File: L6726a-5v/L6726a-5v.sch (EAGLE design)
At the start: 28 parts, among them IC1 L6727A, U1 5V

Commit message: finalized layout, I think I'm happy
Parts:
- removed U1: 5V, SparkFun-PowerIC:V_REG_317SMD
- added IC2: MCP1804, microchip-vreg:MCP1804
- CVRIN, CVROUT: value (none) -> 1u; device rcl:C-EUC1206 -> rcl:C-EUC0603
- LS: value N_MOSFET_POWERSO8 -> MOSFET-NCH-FDS6630A; device power-mosfet:N_MOSFET_POWERSO8 -> SparkFun-DiscreteSemi:MOSFET-NCH-FDS6630A
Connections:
- net +12V: now also IC2.VIN, IC2.|SHDN; no longer U1.IN
- net GND: now also IC2.GND; no longer U1.ADJ
- net VCC: now also IC2.VOUT; no longer U1.OUT
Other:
- moved on the sheet: CVRIN, CVROUT

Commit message: finishing touches
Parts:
- IC1: value L6727A -> L6726A; device stm-l6727a:L6727A -> stm-l6726a:L6726A
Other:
- note added: "1"
- note added: "Synchronous buck converter based on STM L6726a Controller (C) 2022 G. MCLELLAN"
- moved on the sheet: CBOOT, CBULK1, CBULK2, CBULK3, CBULK4, CC, CDEC, CHF, COUT1, COUT2, CP, CSN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

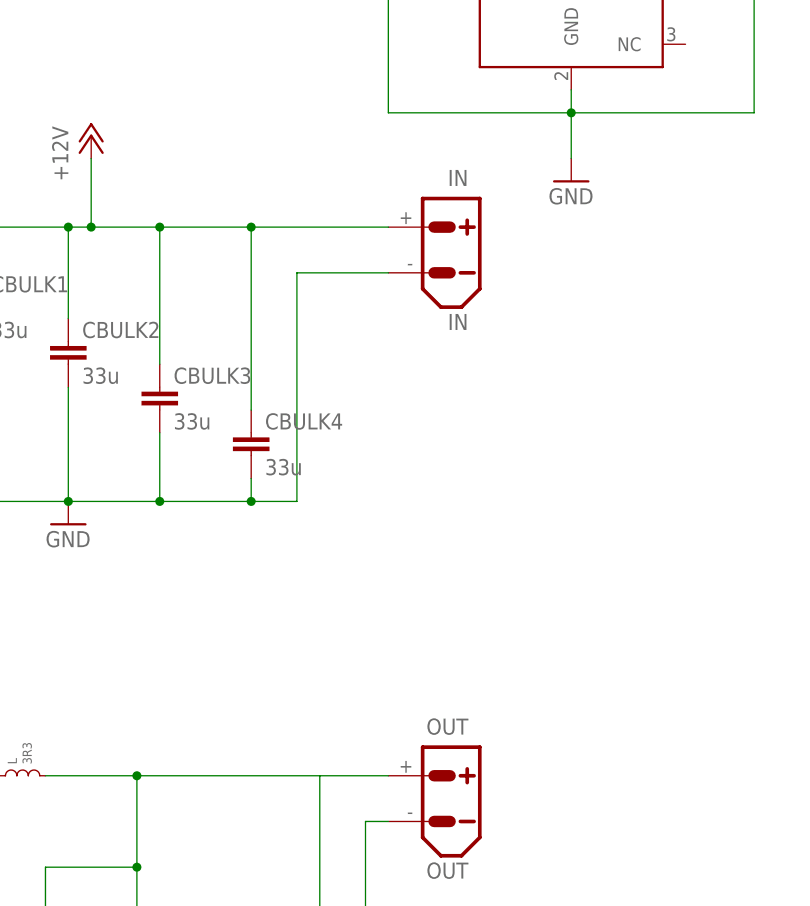
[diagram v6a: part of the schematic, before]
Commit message: let the ground pour through between inductor
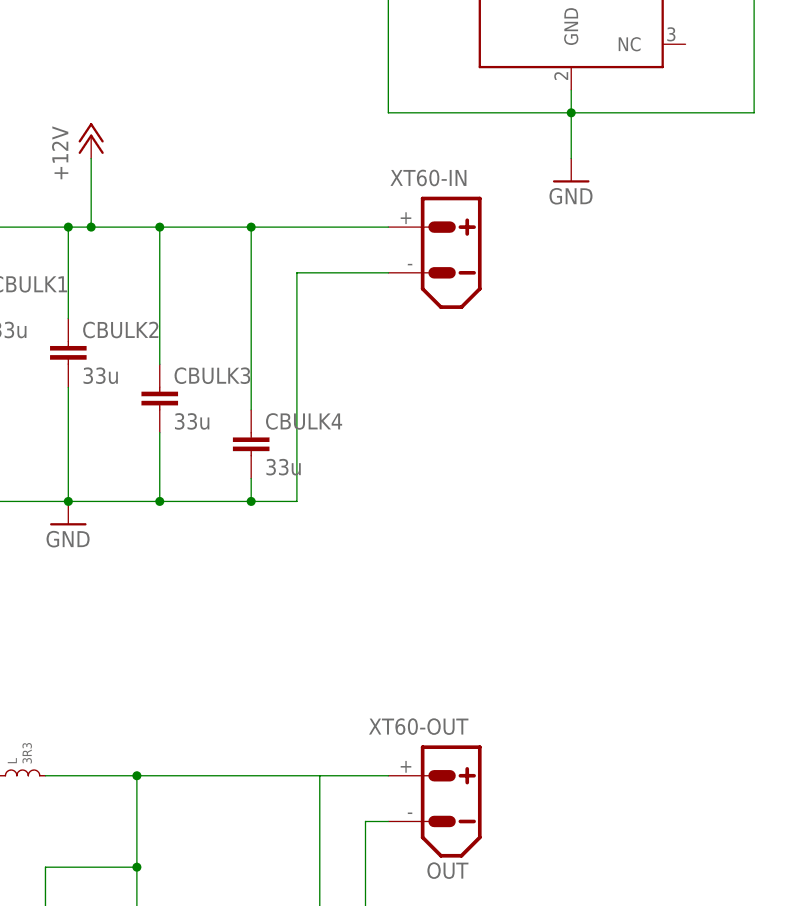
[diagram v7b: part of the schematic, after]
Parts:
- XT60-IN: value IN -> XT60PW-M
- renumbered IN to XT60-IN, OUT to XT60-OUT
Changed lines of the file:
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@@
 <grid distance="0.1" unitdist="inch" unit="inch" style="lines" multiple="1" display="no" altdistance="0.01" altunitdist="inch" altunit="inch"/>
 <layers>
-<layer number="1" name="Top" color="4" fill="1" visible="yes" active="no"/>
-<layer number="16" name="Bottom" color="1" fill="1" visible="yes" active="no"/>
-<layer number="17" name="Pads" color="2" fill="1" visible="yes" active="no"/>
-<layer number="18" name="Vias" color="2" fill="1" visible="yes" active="no"/>
-<layer number="19" name="Unrouted" color="6" fill="1" visible="yes" active="no"/>
-<layer number="20" name="Dimension" color="15" fill="1" visible="yes" active="no"/>
-<layer number="21" name="tPlace" color="7" fill="1" visible="yes" active="no"/>
-<layer number="22" name="bPlace" color="7" fill="1" visible="yes" active="no"/>
-<layer number="23" name="tOrigins" color="15" fill="1" visible="yes" active="no"/>
-<layer number="24" name="bOrigins" color="15" fill="1" visible="yes" active="no"/>
-<layer number="25" name="tNames" color="14" fill="1" visible="yes" active="no"/>
-<layer number="26" name="bNames" color="13" fill="1" visible="yes" active="no"/>
-<layer number="27" name="tValues" color="6" fill="1" visible="yes" active="no"/>
-<layer number="28" name="bValues" color="5" fill="1" visible="yes" active="no"/>
+<layer number="1" name="Top" color="4" fill="1" visible="no" active="no"/>
+<layer number="16" name="Bottom" color="1" fill="1" visible="no" active="no"/>
+<layer number="17" name="Pads" color="2" fill="1" visible="no" active="no"/>
+<layer number="18" name="Vias" color="2" fill="1" visible="no" active="no"/>
+<layer number="19" name="Unrouted" color="6" fill="1" visible="no" active="no"/>
+<layer number="20" name="Dimension" color="15" fill="1" visible="no" active="no"/>
+<layer number="21" name="tPlace" color="7" fill="1" visible="no" active="no"/>
+<layer number="22" name="bPlace" color="7" fill="1" visible="no" active="no"/>
+<layer number="23" name="tOrigins" color="15" fill="1" visible="no" active="no"/>
+<layer number="24" name="bOrigins" color="15" fill="1" visible="no" active="no"/>
+<layer number="25" name="tNames" color="14" fill="1" visible="no" active="no"/>
+<layer number="26" name="bNames" color="13" fill="1" visible="no" active="no"/>
+<layer number="27" name="tValues" color="6" fill="1" visible="no" active="no"/>
+<layer number="28" name="bValues" color="5" fill="1" visible="no" active="no"/>
 <layer number="29" name="tStop" color="7" fill="3" visible="no" active="no"/>
 <layer number="30" name="bStop" color="7" fill="6" visible="no" active="no"/>
@@
 <layer number="35" name="tGlue" color="7" fill="4" visible="no" active="no"/>
 <layer number="36" name="bGlue" color="7" fill="5" visible="no" active="no"/>
-<layer number="37" name="tTest" color="7" fill="1" visible="yes" active="no"/>
-<layer number="38" name="bTest" color="7" fill="1" visible="yes" active="no"/>
+<layer number="37" name="tTest" color="7" fill="1" visible="no" active="no"/>
+<layer number="38" name="bTest" color="7" fill="1" visible="no" active="no"/>
 <layer number="39" name="tKeepout" color="4" fill="11" visible="no" active="no"/>
 <layer number="40" name="bKeepout" color="1" fill="11" visible="no" active="no"/>
@@
 <layer number="44" name="Drills" color="7" fill="1" visible="no" active="no"/>
 <layer number="45" name="Holes" color="7" fill="1" visible="no" active="no"/>
-<layer number="46" name="Milling" color="3" fill="1" visible="yes" active="no"/>
-<layer number="47" name="Measures" color="7" fill="1" visible="yes" active="no"/>
-<layer number="48" name="Document" color="7" fill="1" visible="yes" active="no"/>
-<layer number="49" name="Reference" color="7" fill="1" visible="yes" active="no"/>
-<layer number="50" name="dxf" color="7" fill="1" visible="yes" active="no"/>
-<layer number="51" name="tDocu" color="7" fill="1" visible="yes" active="no"/>
-<layer number="52" name="bDocu" color="7" fill="1" visible="yes" active="no"/>
-<layer number="53" name="tGND_GNDA" color="7" fill="9" visible="yes" active="no"/>
-<layer number="54" name="bGND_GNDA" color="1" fill="9" visible="yes" active="no"/>
-<layer number="56" name="wert" color="7" fill="1" visible="yes" active="no"/>
-<layer number="57" name="tCAD" color="7" fill="1" visible="yes" active="no"/>
-<layer number="58" name="bCAD" color="7" fill="1" visible="yes" active="no"/>
-<layer number="59" name="tCarbon" color="7" fill="1" visible="yes" active="no"/>
-<layer number="60" name="bCarbon" color="7" fill="1" visible="yes" active="no"/>
+<layer number="46" name="Milling" color="3" fill="1" visible="no" active="no"/>
+<layer number="47" name="Measures" color="7" fill="1" visible="no" active="no"/>
+<layer number="48" name="Document" color="7" fill="1" visible="no" active="no"/>
+<layer number="49" name="Reference" color="7" fill="1" visible="no" active="no"/>
+<layer number="50" name="dxf" color="7" fill="1" visible="no" active="no"/>
+<layer number="51" name="tDocu" color="7" fill="1" visible="no" active="no"/>
+<layer number="52" name="bDocu" color="7" fill="1" visible="no" active="no"/>
+<layer number="53" name="tGND_GNDA" color="7" fill="9" visible="no" active="no"/>
+<layer number="54" name="bGND_GNDA" color="1" fill="9" visible="no" active="no"/>
+<layer number="56" name="wert" color="7" fill="1" visible="no" active="no"/>
+<layer number="57" name="tCAD" color="7" fill="1" visible="no" active="no"/>
+<layer number="58" name="bCAD" color="7" fill="1" visible="no" active="no"/>
+<layer number="59" name="tCarbon" color="7" fill="1" visible="no" active="no"/>
+<layer number="60" name="bCarbon" color="7" fill="1" visible="no" active="no"/>
 <layer number="88" name="SimResults" color="9" fill="1" visible="yes" active="yes"/>
 <layer number="89" name="SimProbes" color="9" fill="1" visible="yes" active="yes"/>
@@
 <part name="RC" library="rcl" deviceset="R-US_" device="R0603" value="18K0"/>
 <part name="GND9" library="supply1" deviceset="GND" device=""/>
-<part name="OUT" library="amass" deviceset="XT60" device="PW-M" value="OUT"/>
-<part name="IN" library="amass" deviceset="XT60" device="PW-M" value="IN"/>
+<part name="XT60-OUT" library="amass" deviceset="XT60" device="PW-M" value="OUT"/>
+<part name="XT60-IN" library="amass" deviceset="XT60" device="PW-M" value=""/>
 <part name="L" library="coilcraft" deviceset="INDUCTOR" device=".XAL1010" value="3R3"/>
 <part name="CBULK1" library="rcl" deviceset="C-EU" device="C2220K" value="33u"/>
@@
 <instance part="RC" gate="G$1" x="55.88" y="83.82" rot="R270"/>
 <instance part="GND9" gate="1" x="213.36" y="48.26"/>
-<instance part="OUT" gate="G$1" x="220.98" y="86.36" rot="MR0"/>
-<instance part="IN" gate="G$1" x="220.98" y="147.32" rot="MR0"/>
+<instance part="XT60-OUT" gate="G$1" x="220.98" y="86.36" rot="MR0"/>
+<instance part="XT60-IN" gate="G$1" x="220.98" y="147.32" rot="MR0"/>
 <instance part="L" gate="G$1" x="175.26" y="88.9"/>
 <instance part="CBULK1" gate="G$1" x="170.18" y="142.24"/>
@@
 <wire x1="190.5" y1="149.86" x2="190.5" y2="134.62" width="0.1524" layer="91"/>
 <junction x="182.88" y="149.86"/>
-<pinref part="IN" gate="G$1" pin="+"/>
+<pinref part="XT60-IN" gate="G$1" pin="+"/>
 <wire x1="215.9" y1="149.86" x2="200.66" y2="149.86" width="0.1524" layer="91"/>
 <junction x="190.5" y="149.86"/>
@@
 <wire x1="190.5" y1="119.38" x2="190.5" y2="127" width="0.1524" layer="91"/>
 <wire x1="180.34" y1="119.38" x2="190.5" y2="119.38" width="0.1524" layer="91"/>
-<pinref part="IN" gate="G$1" pin="-"/>
+<pinref part="XT60-IN" gate="G$1" pin="-"/>
 <wire x1="215.9" y1="144.78" x2="205.74" y2="144.78" width="0.1524" layer="91"/>
 <wire x1="205.74" y1="144.78" x2="205.74" y2="119.38" width="0.1524" layer="91"/>
@@
 <wire x1="215.9" y1="83.82" x2="213.36" y2="83.82" width="0.1524" layer="91"/>
 <wire x1="213.36" y1="83.82" x2="213.36" y2="50.8" width="0.1524" layer="91"/>
-<pinref part="OUT" gate="G$1" pin="-"/>
+<pinref part="XT60-OUT" gate="G$1" pin="-"/>
 </segment>
 <segment>
@@
 <wire x1="177.8" y1="88.9" x2="187.96" y2="88.9" width="0.1524" layer="91"/>
 <junction x="187.96" y="88.9"/>
-<pinref part="OUT" gate="G$1" pin="+"/>
+<pinref part="XT60-OUT" gate="G$1" pin="+"/>
 <pinref part="L" gate="G$1" pin="2"/>
 </segment>

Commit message: a few more tweaks!
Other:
- note added: "15-28VDC"
- note added: "5V 25A"
- note added: "5V LDO"
- note added: "Feedback voltage divider"
- moved on the sheet: CDEC, CVRIN, CVROUT, HS, LS
